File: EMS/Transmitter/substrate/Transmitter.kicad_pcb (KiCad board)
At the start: 2 copper layers, 60 x 60 mm, 12 parts

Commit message: :construction: WIP
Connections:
- L pad 4: Net-(J2-Pad2) -> Net-(J1-Pad2)
- R pad 3: Net-(J2-Pad1) -> Net-(J1-Pad1)
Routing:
- net Net-(J1-Pad1): track 0.00 -> 58.8 mm
- net Net-(J2-Pad1): track 58.4 -> 0.00 mm
- net Net-(J2-Pad2): track 36.7 -> 0.00 mm
- net Net-(J1-Pad2): track 0.00 -> 36.4 mm
- net Net-(J1-Pad7): track 48.8 -> 45.7 mm
- net GND: track 125.4 -> 123.0 mm
- net Net-(J1-Pad6): track 53.5 -> 51.4 mm

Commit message: 基板の更新
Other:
- board text added: "EMS-Transmitter ICHINOSEKI"
- board text removed: "ICHINOSEKI-B EMS Transmitter 2021 Falco"

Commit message: Update transmitter.
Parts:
- removed I2C: I2C, Connector_JST:JST_XH_S4B-XH-A_1x04_P2.50mm_Horizontal
- removed L: Pico_Left, Connector_PinSocket_2.54mm:PinSocket_1x20_P2.54mm_Vertical
- removed R: Pico_Right, Connector_PinSocket_2.54mm:PinSocket_1x20_P2.54mm_Vertical
- removed the REF** at (176.4, 134.6)
- removed the REF** at (176.4, 79.6)
- removed the REF** at (121.4, 79.6)
- removed the REF** at (121.4, 134.6)
- added R1: 18Ω, Resistor_THT:R_Axial_DIN0207_L6.3mm_D2.5mm_P7.62mm_Horizontal, F.Cu at (157.0, 97.6)
- added R2: 18Ω, Resistor_THT:R_Axial_DIN0207_L6.3mm_D2.5mm_P7.62mm_Horizontal, F.Cu at (161.0, 97.6)
- added R3: 18Ω, Resistor_THT:R_Axial_DIN0207_L6.3mm_D2.5mm_P7.62mm_Horizontal, F.Cu at (155.0, 102.0)
- added REF**: MountingHole_3.2mm_M3_Pad_Via, MountingHole:MountingHole_3.2mm_M3_Pad_Via, F.Cu at (160.0, 109.0)
- added REF**: MountingHole_3.2mm_M3_Pad_Via, MountingHole:MountingHole_3.2mm_M3_Pad_Via, F.Cu at (125.0, 109.0)
- added REF**: MountingHole_3.2mm_M3_Pad_Via, MountingHole:MountingHole_3.2mm_M3_Pad_Via, F.Cu at (160.0, 74.0)
- added REF**: MountingHole_3.2mm_M3_Pad_Via, MountingHole:MountingHole_3.2mm_M3_Pad_Via, F.Cu at (125.0, 74.0)
- added U1: SeeeduinoXIAO, Seeeduino XIAO KICAD:Seeeduino XIAO-MOUDLE14P-2.54-21X17.8MM, F.Cu at (130.0, 99.0)
- J3: renamed from L; value ADP_Left -> ADP_L
- J4: renamed from R; value ADP_Right -> ADP_R
- J6: renamed from EMS; value EMS_IN -> ESS_IN
- moved J5 37.6 mm to (133.0, 104.0), turned to 0 degrees
- moved J3 27.2 mm to (126.3, 79.8), turned to 0 degrees
- moved J6 25.9 mm to (143.0, 104.0), turned to 0 degrees
- moved J4 21.0 mm to (151.7, 79.8), turned to 0 degrees
- moved SW1 7.73 mm to (156.0, 81.0), turned to 0 degrees
- renumbered POWER to J5, SW to SW1
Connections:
- J3 pad 1: Net-(J2-Pad4) -> (no net)
- J3 pad 10: Net-(J2-Pad5) -> (no net)
- J3 pad 2: Net-(J3-Pad2) -> (no net)
- J3 pad 3: Net-(J3-Pad3) -> (no net)
- J3 pad 4: Net-(J1-Pad2) -> RX
- J3 pad 5: Net-(J3-Pad5) -> (no net)
- J3 pad 6: Net-(J3-Pad6) -> (no net)
- J3 pad 7: Net-(J3-Pad7) -> (no net)
- J3 pad 8: Net-(J3-Pad8) -> (no net)
- J3 pad 9: Net-(J2-Pad16) -> +3V3
- J4 pad 1: Net-(J4-Pad1) -> (no net)
- J4 pad 10: Net-(J4-Pad10) -> (no net)
- J4 pad 2: Net-(J4-Pad2) -> (no net)
- J4 pad 3: Net-(J1-Pad1) -> TX
- J4 pad 4: Net-(J4-Pad4) -> (no net)
- J4 pad 5: Net-(J4-Pad5) -> (no net)
- J4 pad 6: Net-(J4-Pad6) -> (no net)
- J4 pad 7: Net-(J4-Pad7) -> (no net)
- J4 pad 8: Net-(J4-Pad8) -> (no net)
- J5 pad 1: +5V -> PW_IN
- J6 pad 1: Net-(J2-Pad7) -> +5V
- J6 pad 2: Net-(J2-Pad6) -> ESS_IN
- SW1 pad 1: Net-(SW1-Pad1) -> +5V
- SW1 pad 2: Net-(J2-Pad19) -> PW_IN
- SW1 pad 3: +5V -> (no net)
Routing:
- net GND: track 123.0 -> 56.4 mm, vias 0 -> 1
- net Net-(J2-Pad19): track 65.1 -> 0.00 mm
- net Net-(J1-Pad1): track 58.8 -> 0.00 mm
- net PW_IN: track 0.00 -> 54.4 mm
- net Net-(J1-Pad6): track 51.4 -> 0.00 mm
- net Net-(J2-Pad16): track 49.8 -> 0.00 mm
- net Net-(J1-Pad7): track 45.7 -> 0.00 mm
- net Net-(J2-Pad4): track 41.4 -> 0.00 mm
- net +5V: track 11.7 -> 49.8 mm
- net ESS_IN: track 0.00 -> 37.1 mm, vias 0 -> 1
- net Net-(J1-Pad2): track 36.4 -> 0.00 mm
- net TX: track 0.00 -> 33.8 mm
- net +3V3: track 0.00 -> 27.7 mm, vias 0 -> 2
- net Net-(J2-Pad7): track 27.6 -> 0.00 mm
- net RX: track 0.00 -> 24.3 mm, vias 0 -> 1
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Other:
- board size 60 x 60 mm -> 43 x 43 mm
- board text removed: "EMS-Transmitter ICHINOSEKI"
- board text removed: "IM920"
- board text removed: "RP-Pico"

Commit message: Modify the PCB and add the Gerber files.
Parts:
- renumbered J5 to 5V, J6 to ESS, SW1 to SW
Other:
- board text added: "RESS-Transmitter 2022 Ichinoseki-B Falco"

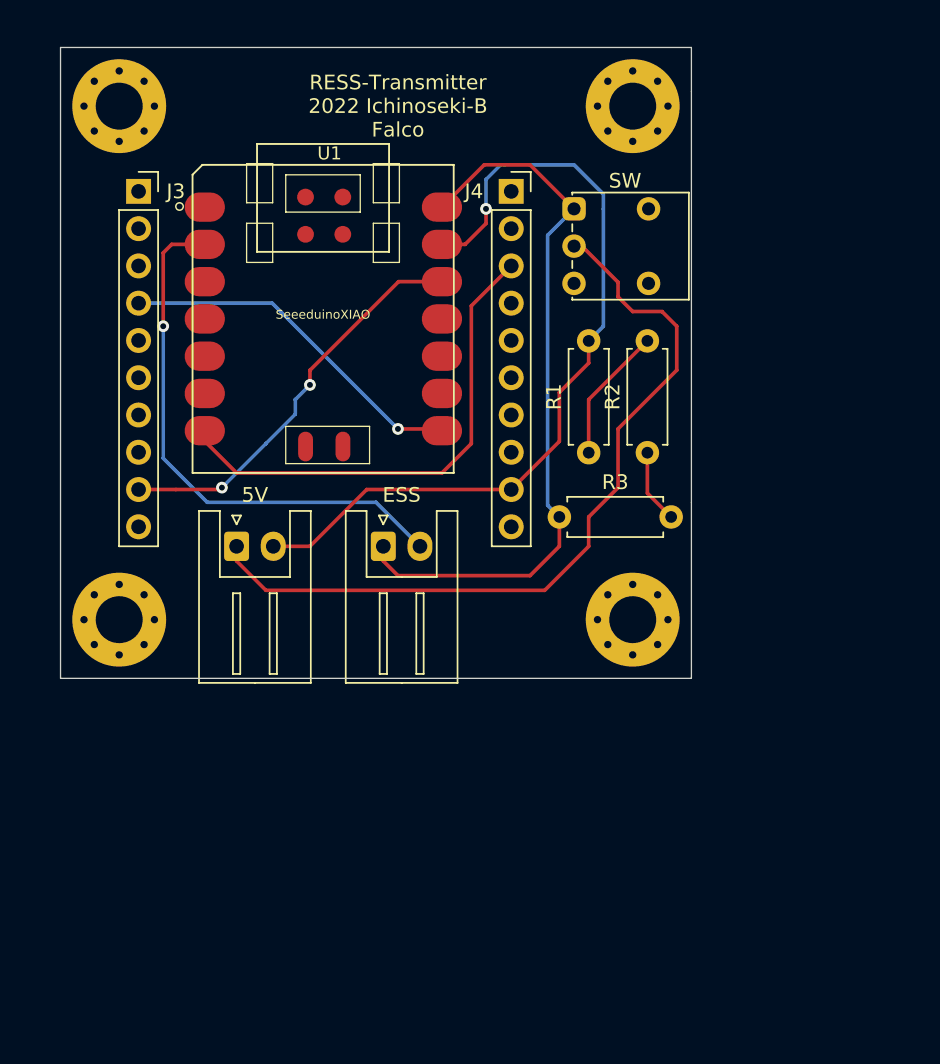
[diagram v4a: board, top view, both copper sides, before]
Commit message: Fix of interference part.
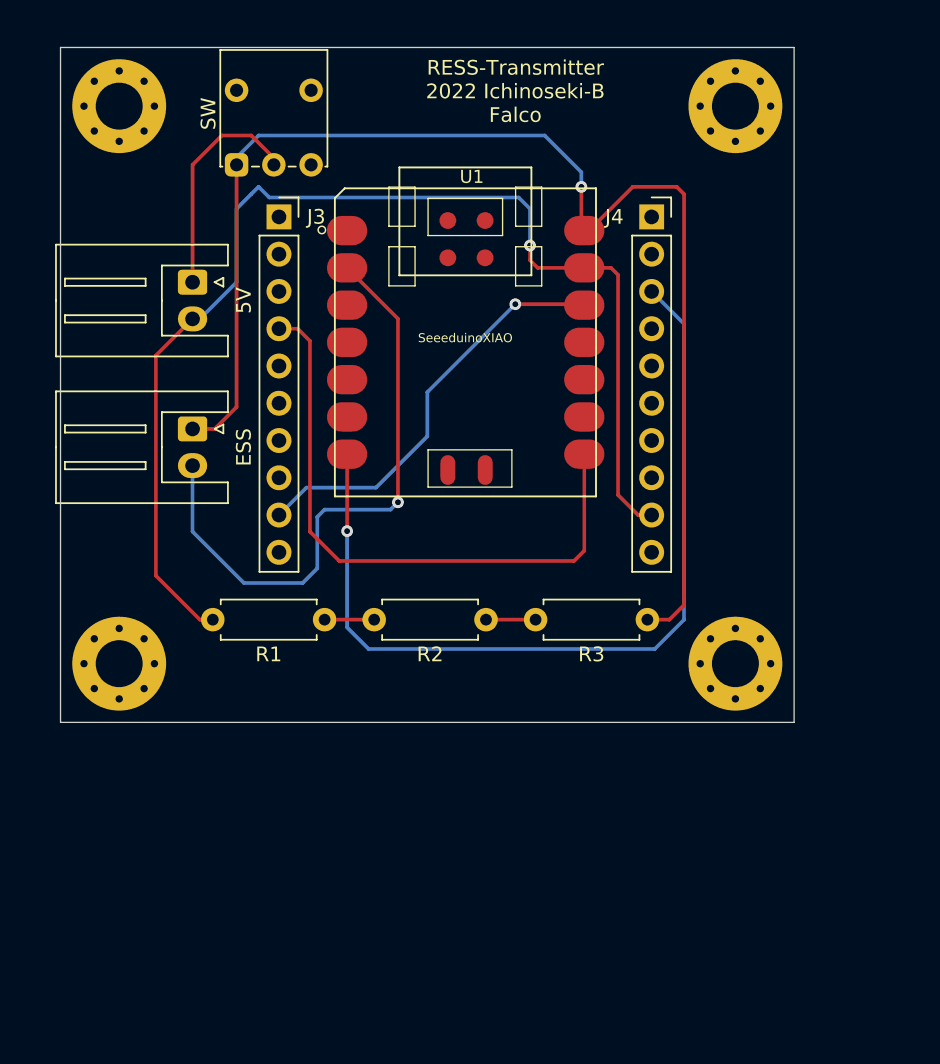
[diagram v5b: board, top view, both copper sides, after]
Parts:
- moved SW 23.2 mm to (133.0, 78.0), turned to 90 degrees
- moved R1 21.3 mm to (139.0, 109.0), turned to 180 degrees
- moved 5V 18.2 mm to (130.0, 86.0), turned to 270 degrees
- moved R2 15.8 mm to (150.0, 109.0), turned to 180 degrees
- moved ESS 15.3 mm to (130.0, 96.0), turned to 270 degrees
- moved U1 9.83 mm to (139.7, 100.6)
- moved J3 9.73 mm to (135.9, 81.5)
- moved J4 9.73 mm to (161.3, 81.5)
- moved R3 9.22 mm to (161.0, 109.0), turned to 180 degrees
- moved REF** 7.62 mm to (167.0, 112.0)
- moved REF** 7.00 mm to (167.0, 74.0)
- moved REF** 3.00 mm to (125.0, 112.0)
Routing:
- net +5V: track 49.8 -> 89.0 mm, vias 0 -> 1
- net PW_IN: track 54.4 -> 15.5 mm
- net TX: track 33.8 -> 59.5 mm, vias 0 -> 1
- net GND: track 56.4 -> 81.7 mm
- net RX: track 24.3 -> 41.8 mm, vias 1 -> 0
- net Net-(R1-Pad1): track 9.28 -> 3.38 mm
- net ESS_IN: track 37.1 -> 41.7 mm
- net Net-(R2-Pad1): track 5.05 -> 3.38 mm
- net +3V3: track 27.7 -> 28.5 mm, vias 2 -> 1
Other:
- board size 43 x 43 mm -> 50 x 46 mm
